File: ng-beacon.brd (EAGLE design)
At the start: 70.9 x 76.3 mm, 2 parts

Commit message: update board layout
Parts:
- moved G1 20.4 mm to (25.4, 50.8)
- moved U$1 11.7 mm to (45.7, 14.0), turned to 180 degrees
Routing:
- net N$1: track 78.4 -> 92.9 mm
- net N$2: track 54.3 -> 64.6 mm
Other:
- board size 70.9 x 76.3 mm -> 71.1 x 76.2 mm
- board text removed: "A"
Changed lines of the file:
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@@
 <board>
 <plain>
-<polygon width="0.254" layer="20" spacing="195.58" pour="hatch">
-<vertex x="45.7962" y="74.9681"/>
-<vertex x="10.287" y="62.3189"/>
-<vertex x="15.6972" y="15.3797"/>
-<vertex x="45.72" y="-1.3081"/>
-<vertex x="75.7428" y="15.3797"/>
-<vertex x="81.153" y="62.3189"/>
-</polygon>
-<text x="24.13" y="16.51" size="50.8" layer="26">A</text>
+<polygon width="0.254" layer="26">
+<vertex x="48.0822" y="60.8076"/>
+<vertex x="48.0822" y="43.942"/>
+<vertex x="52.4002" y="33.6296"/>
+<vertex x="48.0822" y="33.6296"/>
+<vertex x="48.0822" y="26.6192"/>
+<vertex x="55.3466" y="26.6192"/>
+<vertex x="59.9186" y="15.24"/>
+<vertex x="68.3514" y="15.24"/>
+</polygon>
+<polygon width="0.254" layer="25">
+<vertex x="48.0822" y="60.8076"/>
+<vertex x="45.7454" y="66.04"/>
+<vertex x="23.0886" y="15.24"/>
+<vertex x="31.5214" y="15.24"/>
+<vertex x="36.0934" y="26.6192"/>
+<vertex x="48.0822" y="26.6192"/>
+<vertex x="48.0822" y="33.6296"/>
+<vertex x="39.1414" y="33.6296"/>
+<vertex x="45.7454" y="49.53"/>
+<vertex x="48.0822" y="43.942"/>
+</polygon>
+<wire x1="10.16" y1="62.23" x2="45.72" y2="74.93" width="0.4064" layer="20"/>
+<wire x1="45.72" y1="74.93" x2="81.28" y2="62.23" width="0.4064" layer="20"/>
+<wire x1="81.28" y1="62.23" x2="75.565" y2="15.24" width="0.4064" layer="20"/>
+<wire x1="75.565" y1="15.24" x2="45.72" y2="-1.27" width="0.4064" layer="20"/>
+<wire x1="45.72" y1="-1.27" x2="15.875" y2="15.24" width="0.4064" layer="20"/>
+<wire x1="15.875" y1="15.24" x2="10.16" y2="62.23" width="0.4064" layer="20"/>
+<polygon width="0.254" layer="25">
+<vertex x="48.0822" y="60.8076"/>
+<vertex x="48.0822" y="43.942"/>
+<vertex x="52.4002" y="33.6296"/>
+<vertex x="48.0822" y="33.6296"/>
+<vertex x="48.0822" y="26.6192"/>
+<vertex x="55.3466" y="26.6192"/>
+<vertex x="59.9186" y="15.24"/>
+<vertex x="68.3514" y="15.24"/>
+</polygon>
+<polygon width="0" layer="27">
+<vertex x="48.0822" y="60.8076"/>
+<vertex x="45.7454" y="66.04"/>
+<vertex x="23.0886" y="15.24"/>
+<vertex x="31.5214" y="15.24"/>
+<vertex x="36.0934" y="26.6192"/>
+<vertex x="48.0822" y="26.6192"/>
+<vertex x="48.0822" y="33.6296"/>
+<vertex x="39.1414" y="33.6296"/>
+<vertex x="45.7454" y="49.53"/>
+<vertex x="48.0822" y="43.942"/>
+</polygon>
+<polygon width="0.254" layer="26">
+<vertex x="48.0822" y="60.8076"/>
+<vertex x="45.7454" y="66.04"/>
+<vertex x="23.0886" y="15.24"/>
+<vertex x="31.5214" y="15.24"/>
+<vertex x="36.0934" y="26.6192"/>
+<vertex x="48.0822" y="26.6192"/>
+<vertex x="48.0822" y="33.6296"/>
+<vertex x="39.1414" y="33.6296"/>
+<vertex x="45.7454" y="49.53"/>
+<vertex x="48.0822" y="43.942"/>
+</polygon>
 </plain>
 <attributes>
@@
 </class>
 </classes>
-<designrules name="default">
+<designrules name="SeeedStudio_2layer_DRU_no_angle_20140221">
 <description language="de">&lt;b&gt;EAGLE Design Rules&lt;/b&gt;
 &lt;p&gt;
@@
 necessary adjustments and save your customized
 design rules under a new name.</description>
+<description language="zh">&lt;b&gt;Seeed Studio EAGLE Design Rules&lt;/b&gt;
+</description>
 <param name="layerSetup" value="(1*16)"/>
-<param name="mtCopper" value="0.035mm 0.035mm 0.035mm 0.035mm 0.035mm 0.035mm 0.035mm 0.035mm 0.035mm 0.035mm 0.035mm 0.035mm 0.035mm 0.035mm 0.035mm 0.035mm"/>
-<param name="mtIsolate" value="1.5mm 0.15mm 0.2mm 0.15mm 0.2mm 0.15mm 0.2mm 0.15mm 0.2mm 0.15mm 0.2mm 0.15mm 0.2mm 0.15mm 0.2mm"/>
-<param name="mdWireWire" value="8mil"/>
-<param name="mdWirePad" value="8mil"/>
-<param name="mdWireVia" value="8mil"/>
-<param name="mdPadPad" value="8mil"/>
-<param name="mdPadVia" value="8mil"/>
-<param name="mdViaVia" value="8mil"/>
-<param name="mdSmdPad" value="8mil"/>
-<param name="mdSmdVia" value="8mil"/>
-<param name="mdSmdSmd" value="8mil"/>
+<param name="mtCopper" value="0.035mm 0.0175mm 0.035mm 0.035mm 0.035mm 0.035mm 0.035mm 0.035mm 0.035mm 0.035mm 0.035mm 0.035mm 0.035mm 0.035mm 0.0175mm 0.035mm"/>
+<param name="mtIsolate" value="1.5mm 1.1mm 0.2mm 0.15mm 0.2mm 0.15mm 0.2mm 0.15mm 0.2mm 0.15mm 0.2mm 0.15mm 0.2mm 0.15mm 0.2mm"/>
+<param name="mdWireWire" value="6mil"/>
+<param name="mdWirePad" value="6mil"/>
+<param name="mdWireVia" value="6mil"/>
+<param name="mdPadPad" value="6mil"/>
+<param name="mdPadVia" value="6mil"/>
+<param name="mdViaVia" value="6mil"/>
+<param name="mdSmdPad" value="0mil"/>
+<param name="mdSmdVia" value="0mil"/>
+<param name="mdSmdSmd" value="0mil"/>
 <param name="mdViaViaSameLayer" value="8mil"/>
 <param name="mnLayersViaInSmd" value="2"/>
-<param name="mdCopperDimension" value="40mil"/>
-<param name="mdDrill" value="8mil"/>
+<param name="mdCopperDimension" value="10mil"/>
+<param name="mdDrill" value="10mil"/>
 <param name="mdSmdStop" value="0mil"/>
-<param name="msWidth" value="10mil"/>
-<param name="msDrill" value="24mil"/>
-<param name="msMicroVia" value="9.99mm"/>
+<param name="msWidth" value="6mil"/>
+<param name="msDrill" value="12mil"/>
+<param name="msMicroVia" value="12mil"/>
 <param name="msBlindViaRatio" value="0.5"/>
 <param name="rvPadTop" value="0.25"/>
@@
 <param name="rlMinPadBottom" value="10mil"/>
 <param name="rlMaxPadBottom" value="20mil"/>
-<param name="rlMinViaOuter" value="8mil"/>
+<param name="rlMinViaOuter" value="6mil"/>
 <param name="rlMaxViaOuter" value="20mil"/>
-<param name="rlMinViaInner" value="8mil"/>
+<param name="rlMinViaInner" value="6mil"/>
 <param name="rlMaxViaInner" value="20mil"/>
 <param name="rlMinMicroViaOuter" value="4mil"/>
@@
 <param name="psTop" value="-1"/>
 <param name="psBottom" value="-1"/>
-<param name="psFirst" value="-1"/>
+<param name="psFirst" value="0"/>
 <param name="psElongationLong" value="100"/>
 <param name="psElongationOffset" value="100"/>
 <param name="mvStopFrame" value="1"/>
 <param name="mvCreamFrame" value="0"/>
-<param name="mlMinStopFrame" value="4mil"/>
-<param name="mlMaxStopFrame" value="4mil"/>
+<param name="mlMinStopFrame" value="2mil"/>
+<param name="mlMaxStopFrame" value="2mil"/>
 <param name="mlMinCreamFrame" value="0mil"/>
 <param name="mlMaxCreamFrame" value="0mil"/>
-<param name="mlViaStopLimit" value="0mil"/>
+<param name="mlViaStopLimit" value="100mil"/>
 <param name="srRoundness" value="0"/>
 <param name="srMinRoundness" value="0mil"/>
@@
 <param name="checkAngle" value="0"/>
 <param name="checkFont" value="1"/>
-<param name="checkRestrict" value="1"/>
+<param name="checkRestrict" value="0"/>
 <param name="useDiameter" value="13"/>
 <param name="maxErrors" value="50"/>
@@
 </autorouter>
 <elements>
-<element name="G1" library="battery" package="CR2032H" value="CR2032H" x="45.72" y="52.07"/>
-<element name="U$1" library="PTR5518" package="PTR5518" value="PTR5518STD" x="48.26" y="25.4"/>
+<element name="G1" library="battery" package="CR2032H" value="CR2032H" x="25.4" y="50.8"/>
+<element name="U$1" library="PTR5518" package="PTR5518" value="PTR5518STD" x="45.72" y="13.97" rot="R180"/>
 </elements>
 <signals>
@@
 <contactref element="G1" pad="+"/>
 <contactref element="U$1" pad="10"/>
-<wire x1="50.8" y1="62.865" x2="50.8" y2="67.31" width="0.4064" layer="1"/>
-<wire x1="50.8" y1="67.31" x2="49.53" y2="68.58" width="0.4064" layer="1" curve="90"/>
-<wire x1="49.53" y1="68.58" x2="31.75" y2="68.58" width="0.4064" layer="1"/>
-<wire x1="31.75" y1="68.58" x2="30.48" y2="67.31" width="0.4064" layer="1" curve="90"/>
-<wire x1="30.48" y1="67.31" x2="30.48" y2="26.67" width="0.4064" layer="1"/>
-<wire x1="30.48" y1="26.67" x2="31.75" y2="25.4" width="0.4064" layer="1" curve="90"/>
-<wire x1="31.75" y1="25.4" x2="41.91" y2="25.4" width="0.4064" layer="1"/>
+<wire x1="52.07" y1="13.97" x2="68.392746875" y2="13.97" width="0.4064" layer="1"/>
+<wire x1="68.392746875" y1="13.97" x2="69.71225625" y2="15.914321875" width="0.4064" layer="1"/>
+<wire x1="69.71225625" y1="15.914321875" x2="47.69648125" y2="66.942515625" width="0.4064" layer="1"/>
+<wire x1="47.69648125" y1="66.942515625" x2="45.347559375" y2="67.885121875" width="0.4064" layer="1"/>
+<wire x1="45.347559375" y1="67.885121875" x2="30.48" y2="61.595" width="0.4064" layer="1"/>
 </signal>
 <signal name="N$2">
@@
 <contactref element="U$1" pad="9"/>
 <contactref element="U$1" pad="8"/>
-<wire x1="45.72" y1="45.085" x2="33.02" y2="45.085" width="0.4064" layer="1"/>
-<wire x1="33.02" y1="45.085" x2="31.75" y2="43.815" width="0.4064" layer="1" curve="90"/>
-<wire x1="31.75" y1="43.815" x2="31.75" y2="27.94" width="0.4064" layer="1"/>
-<wire x1="31.75" y1="27.94" x2="33.02" y2="26.67" width="0.4064" layer="1" curve="90"/>
-<wire x1="33.02" y1="26.67" x2="41.91" y2="26.67" width="0.4064" layer="1"/>
-<wire x1="41.91" y1="26.67" x2="52.07" y2="26.67" width="0.4064" layer="1"/>
-<wire x1="52.07" y1="26.67" x2="53.34" y2="27.94" width="0.4064" layer="1" curve="-90"/>
-<wire x1="53.34" y1="27.94" x2="54.61" y2="27.94" width="0.4064" layer="1"/>
+<wire x1="25.4" y1="43.815" x2="30.48" y2="36.83" width="0.4064" layer="1"/>
+<wire x1="30.48" y1="36.83" x2="22.262896875" y2="15.70030625" width="0.4064" layer="1"/>
+<wire x1="22.262896875" y1="15.70030625" x2="23.44654375" y2="13.97" width="0.4064" layer="1"/>
+<wire x1="23.44654375" y1="13.97" x2="32.4203875" y2="13.97" width="0.4064" layer="1"/>
+<wire x1="32.4203875" y1="13.97" x2="33.02" y2="11.43" width="0.4064" layer="1"/>
+<wire x1="33.02" y1="11.43" x2="39.37" y2="11.43" width="0.4064" layer="1"/>
+<wire x1="39.37" y1="11.43" x2="44.45" y2="11.43" width="0.4064" layer="1"/>
+<wire x1="44.45" y1="11.43" x2="45.72" y2="12.7" width="0.4064" layer="1"/>
+<wire x1="45.72" y1="12.7" x2="52.07" y2="12.7" width="0.4064" layer="1"/>
+</signal>
+<signal name="N$3">
+<via x="45.72" y="70.485" extent="1-16" drill="2.2"/>
 </signal>
 </signals>

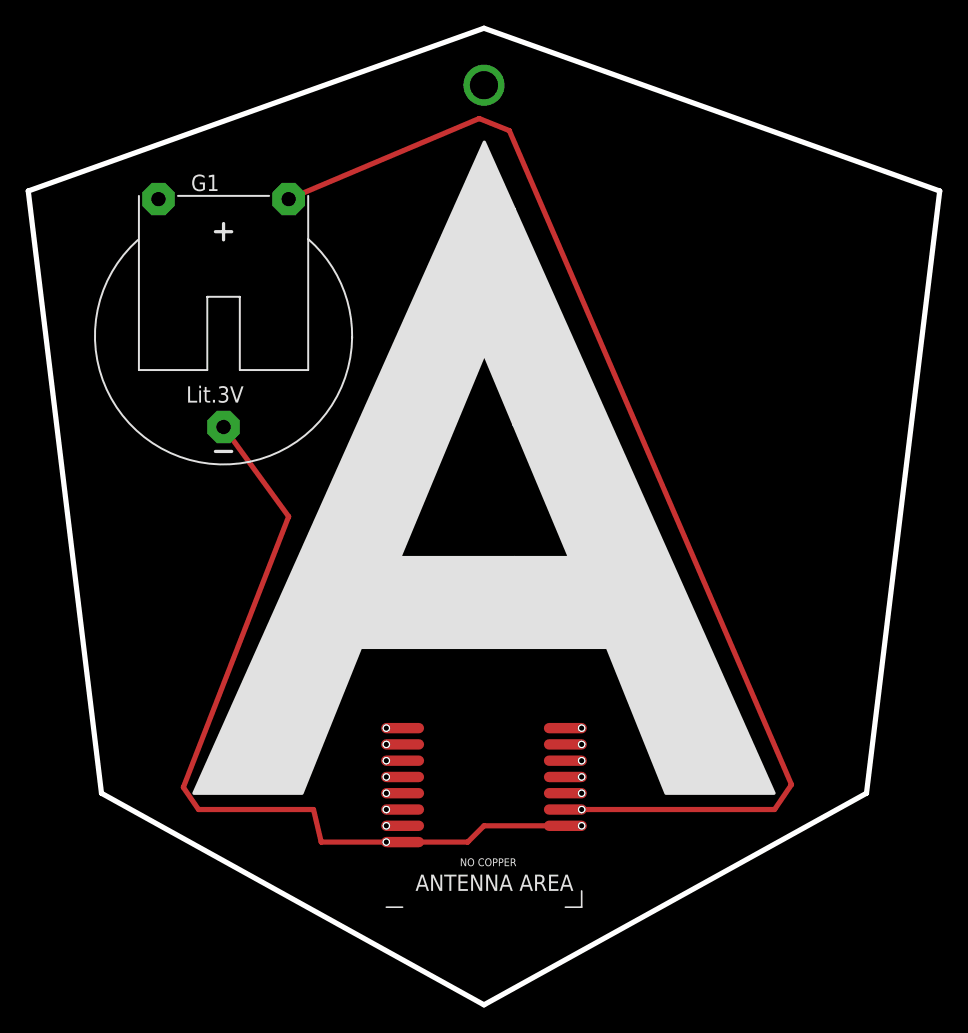
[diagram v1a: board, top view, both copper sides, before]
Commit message: add switch
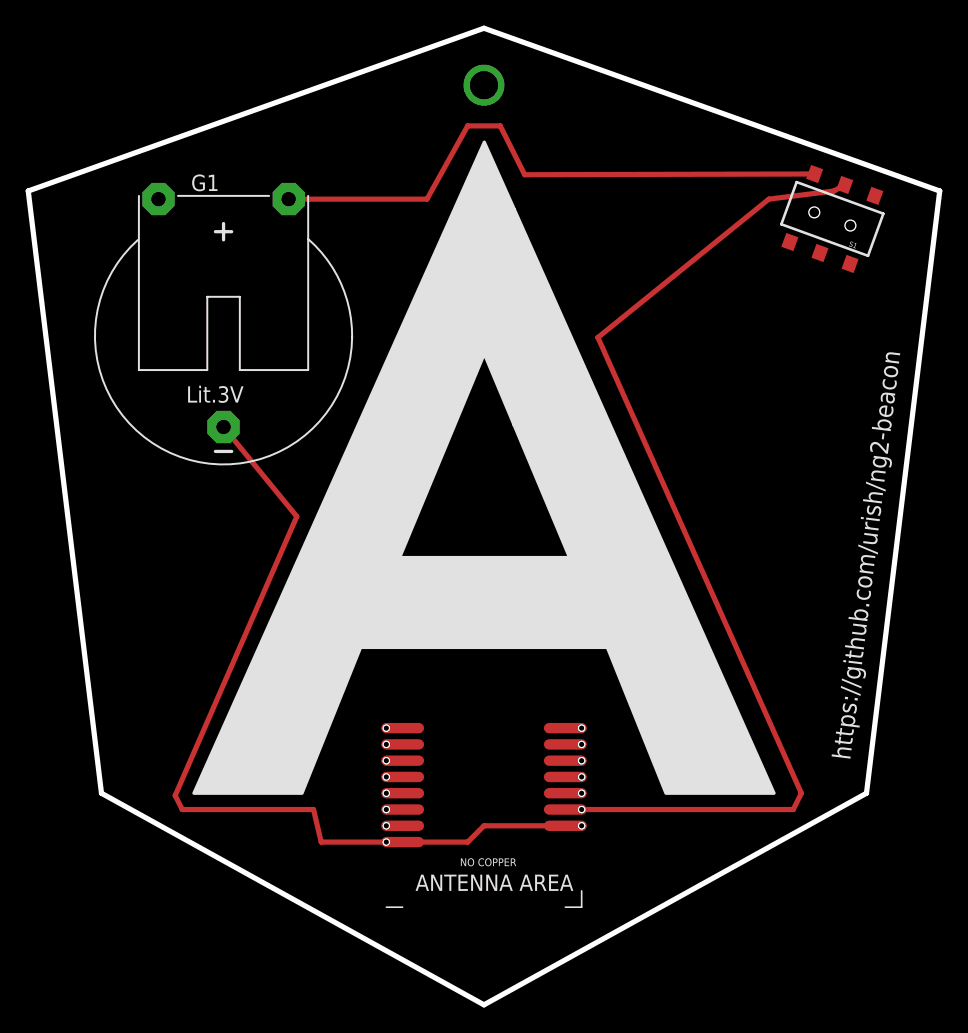
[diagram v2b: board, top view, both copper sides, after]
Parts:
- added S1: DPDT, SparkFun-Electromechanical:AYZ0202
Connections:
- net N$2 renamed GND
- new net VIN: S1.5, U$1.10
- net N$1: now also S1.6; no longer U$1.10
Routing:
- net VIN: track 0.00 -> 81.4 mm
- net N$1: track 92.9 -> 46.8 mm
- net GND: track 64.6 -> 66.4 mm
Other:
- board text added: "https://github.com/urish/ng2-beacon"

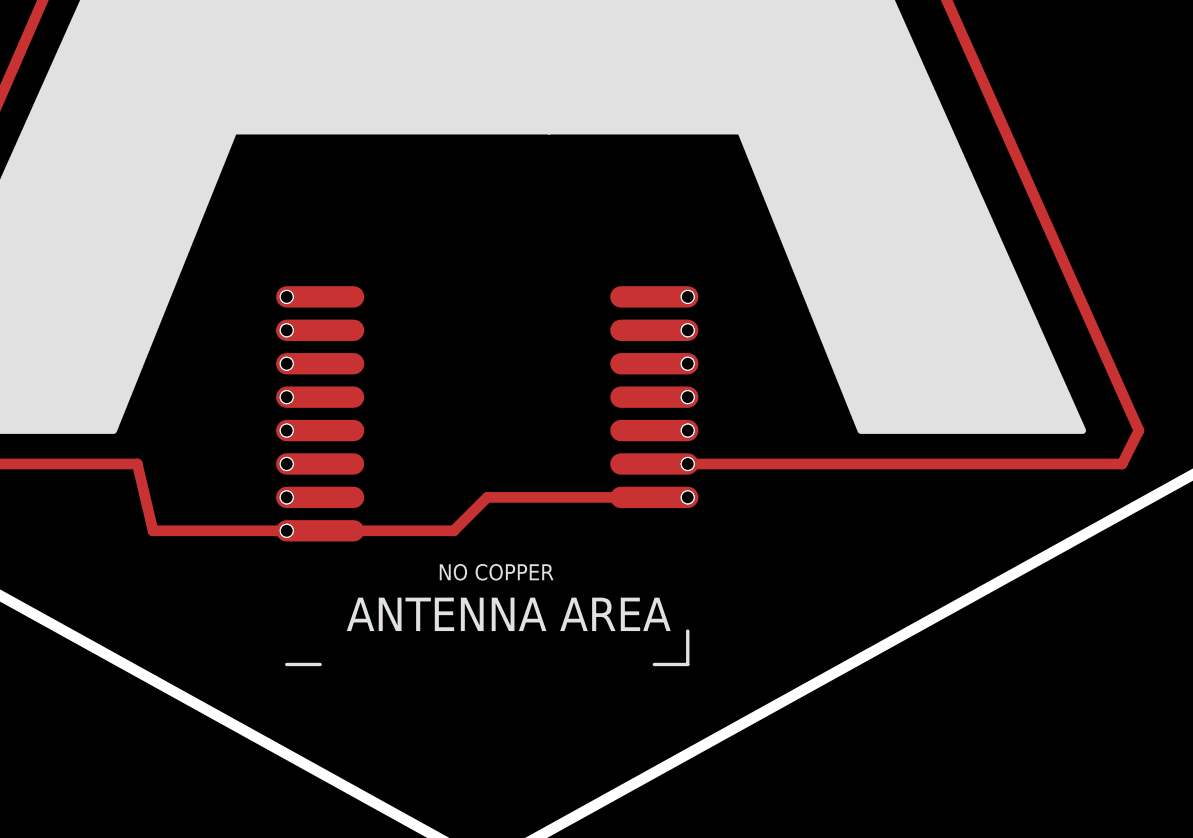
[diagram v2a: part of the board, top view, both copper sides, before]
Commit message: add programming port
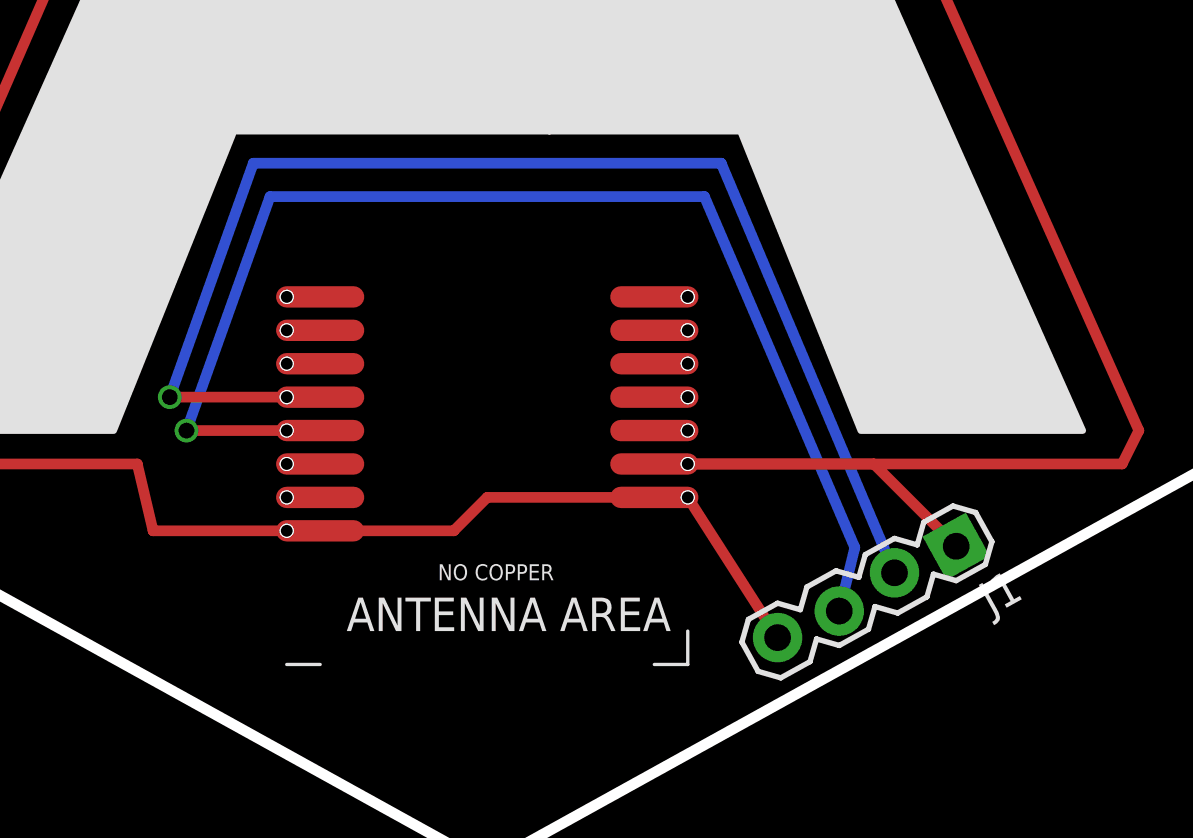
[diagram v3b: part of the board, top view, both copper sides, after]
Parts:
- added J1: (no value), SparkFun-Connectors:1X04_LOCK
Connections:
- new net SWCLK: J1.3, U$1.5
- new net SWDIO: J1.2, U$1.4
- net GND: now also J1.4
- net VIN: now also J1.1
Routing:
- net SWDIO: track 0.00 -> 49.8 mm, vias 0 -> 1
- net SWCLK: track 0.00 -> 48.0 mm, vias 0 -> 1
- net VIN: track 81.4 -> 94.2 mm
- net GND: track 66.4 -> 74.0 mm
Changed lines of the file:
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@@
 <layer number="112" name="tSilk" color="7" fill="1" visible="yes" active="yes"/>
 <layer number="113" name="IDFDebug" color="4" fill="1" visible="yes" active="yes"/>
+<layer number="114" name="Badge_Outline" color="7" fill="1" visible="yes" active="yes"/>
+<layer number="115" name="ReferenceISLANDS" color="7" fill="1" visible="yes" active="yes"/>
 <layer number="116" name="Patch_BOT" color="9" fill="4" visible="yes" active="yes"/>
 <layer number="118" name="Rect_Pads" color="7" fill="1" visible="yes" active="yes"/>
@@
 <attribute name="PROD_ID" value="SWCH-08179" x="72.900953125" y="60.047775" size="1.778" layer="27" rot="R160" display="off"/>
 </element>
+<element name="J1" library="SparkFun-Connectors" package="1X04_LOCK" value="" x="63.48070625" y="10.954234375" rot="R209">
+<attribute name="PROD_ID" value="CONN-09696" x="63.48070625" y="10.954234375" size="1.778" layer="27" rot="R209" display="off"/>
+</element>
 </elements>
 <signals>
@@
 <wire x1="33.02" y1="11.43" x2="39.37" y2="11.43" width="0.4064" layer="1"/>
 <wire x1="45.72" y1="12.7" x2="52.07" y2="12.7" width="0.4064" layer="1"/>
+<contactref element="J1" pad="4"/>
+<wire x1="56.75453125" y1="7.371059375" x2="53.34" y2="12.7" width="0.4064" layer="1"/>
+<wire x1="53.34" y1="12.7" x2="52.07" y2="12.7" width="0.4064" layer="1"/>
 </signal>
 <signal name="N$1">
@@
 <wire x1="73.867159375" y1="62.70240625" x2="73.025" y2="62.23" width="0.4064" layer="1"/>
 <wire x1="73.025" y1="62.23" x2="67.945" y2="61.595" width="0.4064" layer="1"/>
+<contactref element="J1" pad="1"/>
+<wire x1="52.07" y1="13.97" x2="60.41543125" y2="13.97" width="0.4064" layer="1"/>
+<wire x1="60.41543125" y1="13.97" x2="63.542275" y2="10.84315625" width="0.4064" layer="1"/>
+</signal>
+<signal name="SWCLK">
+<contactref element="J1" pad="3"/>
+<contactref element="U$1" pad="5"/>
+<wire x1="59.09920625" y1="8.380321875" x2="59.69" y2="10.795" width="0.4064" layer="16"/>
+<wire x1="59.69" y1="10.795" x2="53.975" y2="24.13" width="0.4064" layer="16"/>
+<wire x1="53.975" y1="24.13" x2="37.465" y2="24.13" width="0.4064" layer="16"/>
+<wire x1="37.465" y1="24.13" x2="34.29" y2="15.24" width="0.4064" layer="16"/>
+<via x="34.29" y="15.24" extent="1-16" drill="0.6" shape="square"/>
+<wire x1="34.29" y1="15.24" x2="39.37" y2="15.24" width="0.4064" layer="1"/>
+</signal>
+<signal name="SWDIO">
+<contactref element="J1" pad="2"/>
+<contactref element="U$1" pad="4"/>
+<wire x1="61.1976" y1="9.83389375" x2="54.61" y2="25.4" width="0.4064" layer="16"/>
+<wire x1="54.61" y1="25.4" x2="36.83" y2="25.4" width="0.4064" layer="16"/>
+<wire x1="36.83" y1="25.4" x2="33.655" y2="16.51" width="0.4064" layer="16"/>
+<via x="33.655" y="16.51" extent="1-16" drill="0.6" shape="square"/>
+<wire x1="33.655" y1="16.51" x2="39.37" y2="16.51" width="0.4064" layer="1"/>
 </signal>
 </signals>
